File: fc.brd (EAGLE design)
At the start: 55 x 40 mm, 72 parts, among them IC1 BN055, J1 USBC, U1 LMZ21700, U2 ATMEGA2560-16AU100A-M, U4 FT230XQ, Y1 16MHz, Y2 32.768kHz

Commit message: led placement on grid
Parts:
- moved LED8 5.00 mm to (16.0, 4.00)
- moved R18 5.00 mm to (16.0, 7.00)
- moved LED7 4.90 mm to (14.0, 4.00)
- moved R17 4.90 mm to (14.0, 7.00)
- moved LED6 4.80 mm to (12.0, 4.00)
- moved R16 4.80 mm to (12.0, 7.00)
- moved LED5 4.70 mm to (10.0, 4.00)
- moved R15 4.70 mm to (10.0, 7.00)
- moved LED4 4.60 mm to (8.00, 4.00)
- moved R14 4.60 mm to (8.00, 7.00)
- moved LED3 4.50 mm to (6.00, 4.00)
- moved R13 4.50 mm to (6.00, 7.00)
- moved LED2 4.40 mm to (4.00, 4.00)
- moved R12 4.40 mm to (4.00, 7.00)
- moved LED1 4.30 mm to (2.00, 4.00)
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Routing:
- net N$31: track 1.40 -> 0.00 mm
- net N$29: track 1.40 -> 0.00 mm
- net N$27: track 1.40 -> 0.00 mm
- net N$24: track 1.40 -> 0.00 mm
- net N$22: track 1.40 -> 0.00 mm
- net N$20: track 1.40 -> 0.00 mm
- net N$18: track 1.40 -> 0.00 mm
- net N$15: track 1.40 -> 0.00 mm
- net LED1: track 38.6 -> 37.7 mm
- net LED7: track 46.2 -> 45.3 mm
- net LED6: track 45.0 -> 44.1 mm
- net LED5: track 43.7 -> 42.8 mm
- net LED4: track 42.4 -> 41.5 mm
- net LED3: track 41.1 -> 40.2 mm
- net LED2: track 39.9 -> 39.0 mm
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
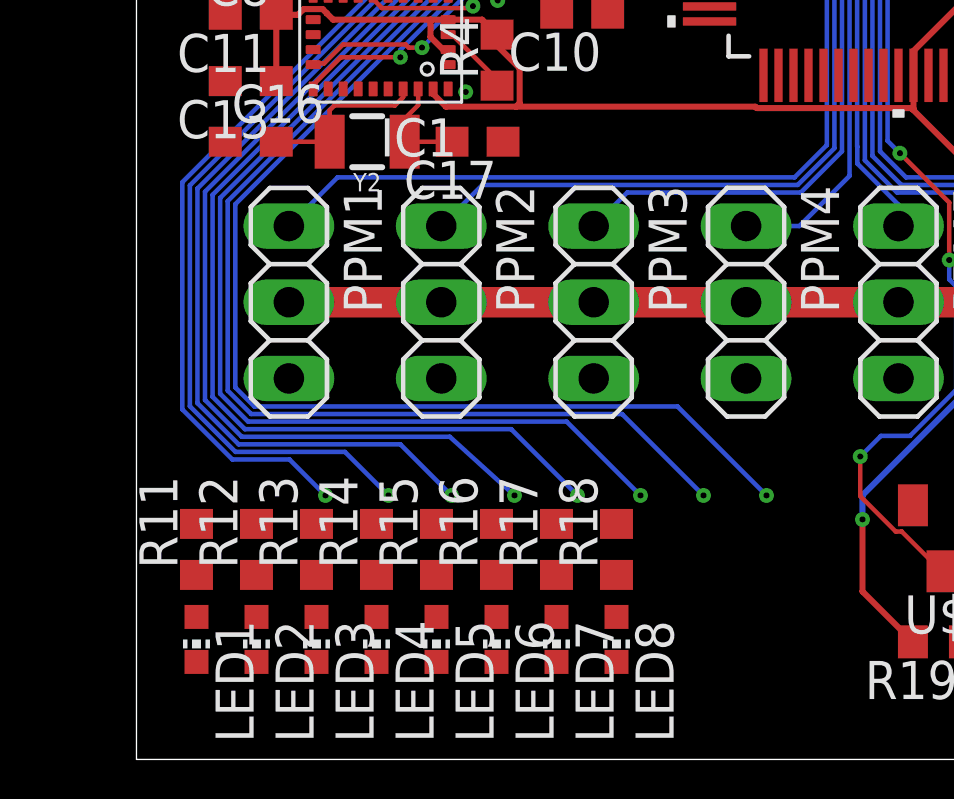
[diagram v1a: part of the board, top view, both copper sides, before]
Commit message: connected LEDs
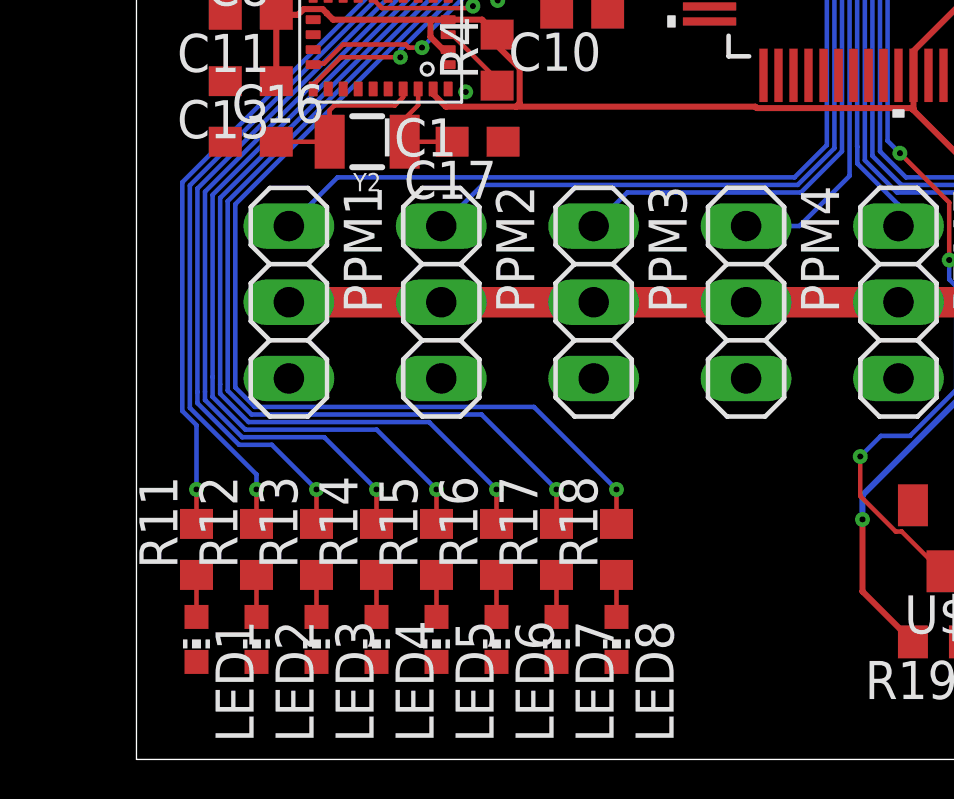
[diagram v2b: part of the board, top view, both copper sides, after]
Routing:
- net LED7: track 45.3 -> 41.4 mm
- net LED6: track 44.1 -> 40.2 mm
- net LED5: track 42.8 -> 39.0 mm
- net LED4: track 41.5 -> 37.9 mm
- net LED3: track 40.2 -> 36.7 mm
- net LED2: track 39.0 -> 35.5 mm
- net LED1: track 37.7 -> 34.7 mm
- net LED0: track 36.4 -> 34.5 mm
- net N$31: track 0.00 -> 1.40 mm
- net N$29: track 0.00 -> 1.40 mm
- net N$27: track 0.00 -> 1.40 mm
- net N$24: track 0.00 -> 1.40 mm
- net N$22: track 0.00 -> 1.40 mm
- net N$20: track 0.00 -> 1.40 mm
- net N$18: track 0.00 -> 1.40 mm
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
